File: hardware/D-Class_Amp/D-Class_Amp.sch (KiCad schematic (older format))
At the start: 17 parts, among them J101 AudioJack2, U101 NCP1117-12_TO252, U102 MCP1799T-5002H_TT

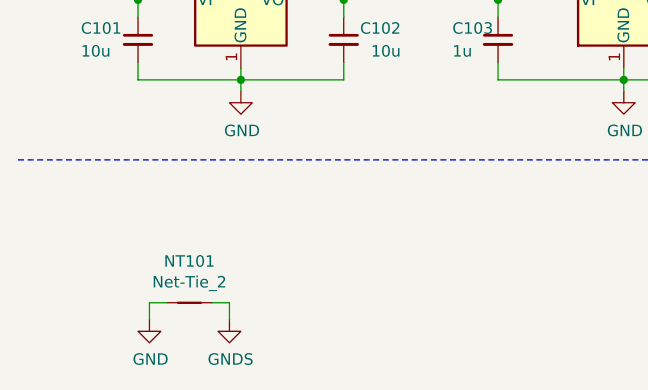
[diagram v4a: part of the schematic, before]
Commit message: updated fet footprints, and added power stage test points
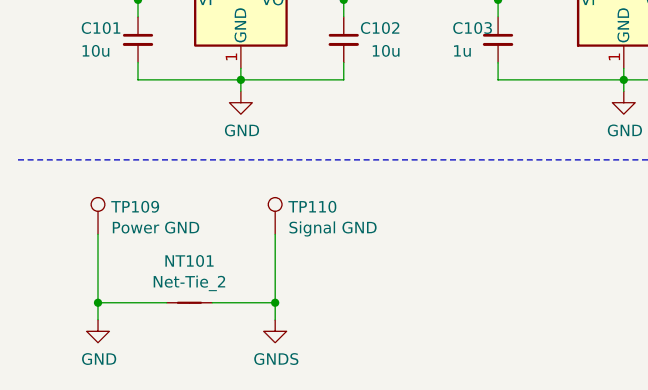
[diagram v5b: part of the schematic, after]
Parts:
- added TP109: Power GND, TestPoint:TestPoint_THTPad_D2.0mm_Drill1.0mm, symbol Connector:TestPoint
- added TP110: Signal GND, TestPoint:TestPoint_THTPad_D2.0mm_Drill1.0mm, symbol Connector:TestPoint
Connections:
- net GND: now also TP109.1
- net GNDS: now also TP110.1
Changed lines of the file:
@@
 L power:GNDS #PWR0102
 U 1 1 612A4FBB
-P 1400 2675
-F 0 "#PWR0102" H 1400 2425 50  0001 C CNN
-F 1 "GNDS" H 1405 2502 50  0000 C CNN
-F 2 "" H 1400 2675 50  0001 C CNN
-F 3 "" H 1400 2675 50  0001 C CNN
-	1    1400 2675
+P 1600 2675
+F 0 "#PWR0102" H 1600 2425 50  0001 C CNN
+F 1 "GNDS" H 1605 2502 50  0000 C CNN
+F 2 "" H 1600 2675 50  0001 C CNN
+F 3 "" H 1600 2675 50  0001 C CNN
+	1    1600 2675
 	1    0    0    -1
 $EndComp
@@
 L power:GND #PWR0101
 U 1 1 612A56C1
-P 1050 2675
-F 0 "#PWR0101" H 1050 2425 50  0001 C CNN
-F 1 "GND" H 1055 2502 50  0000 C CNN
-F 2 "" H 1050 2675 50  0001 C CNN
-F 3 "" H 1050 2675 50  0001 C CNN
-	1    1050 2675
+P 825 2675
+F 0 "#PWR0101" H 825 2425 50  0001 C CNN
+F 1 "GND" H 830 2502 50  0000 C CNN
+F 2 "" H 825 2675 50  0001 C CNN
+F 3 "" H 825 2675 50  0001 C CNN
+	1    825  2675
 	1    0    0    -1
 $EndComp
@@
 $EndComp
 Wire Wire Line
-	1050 2675 1050 2600
-Wire Wire Line
-	1050 2600 1125 2600
-Wire Wire Line
-	1325 2600 1400 2600
-Wire Wire Line
-	1400 2600 1400 2675
+	825  2675 825  2600
+Wire Wire Line
+	825  2600 1125 2600
+Wire Wire Line
+	1325 2600 1600 2600
+Wire Wire Line
+	1600 2600 1600 2675
 $Comp
 L Connector:TestPoint TP101
@@
 Wire Notes Line
 	475  1975 11250 1975
+$Comp
+L Connector:TestPoint TP109
+U 1 1 6113B2E7
+P 825 2300
+F 0 "TP109" H 883 2418 50  0000 L CNN
+F 1 "Power GND" H 883 2327 50  0000 L CNN
+F 2 "TestPoint:TestPoint_THTPad_D2.0mm_Drill1.0mm" H 1025 2300 50  0001 C CNN
+F 3 "~" H 1025 2300 50  0001 C CNN
+	1    825  2300
+	1    0    0    -1
+$EndComp
+$Comp
+L Connector:TestPoint TP110
+U 1 1 6113B863
+P 1600 2300
+F 0 "TP110" H 1658 2418 50  0000 L CNN
+F 1 "Signal GND" H 1658 2327 50  0000 L CNN
+F 2 "TestPoint:TestPoint_THTPad_D2.0mm_Drill1.0mm" H 1800 2300 50  0001 C CNN
+F 3 "~" H 1800 2300 50  0001 C CNN
+	1    1600 2300
+	1    0    0    -1
+$EndComp
+Wire Wire Line
+	825  2300 825  2600
+Connection ~ 825  2600
+Wire Wire Line
+	1600 2300 1600 2600
+Connection ~ 1600 2600
 $EndSCHEMATC

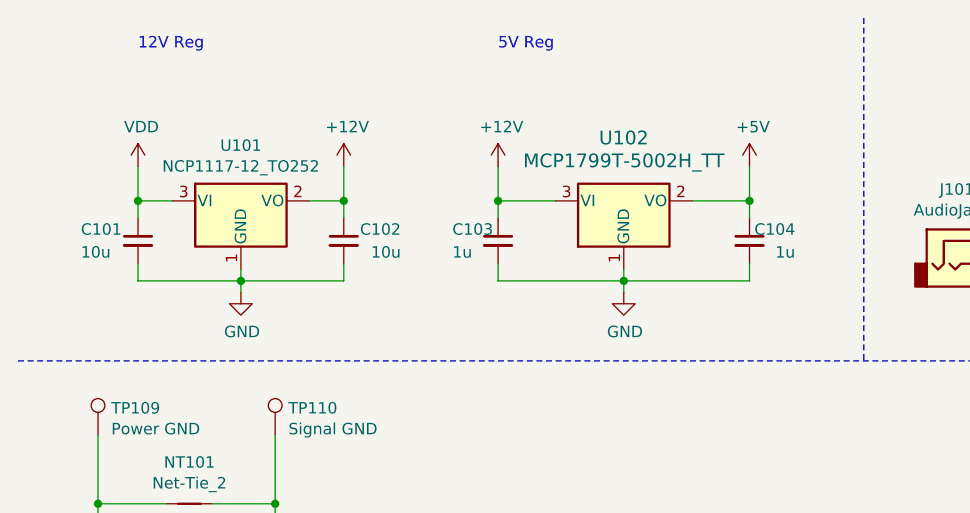
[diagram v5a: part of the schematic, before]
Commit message: Add footprints to the output filter and select output filter components
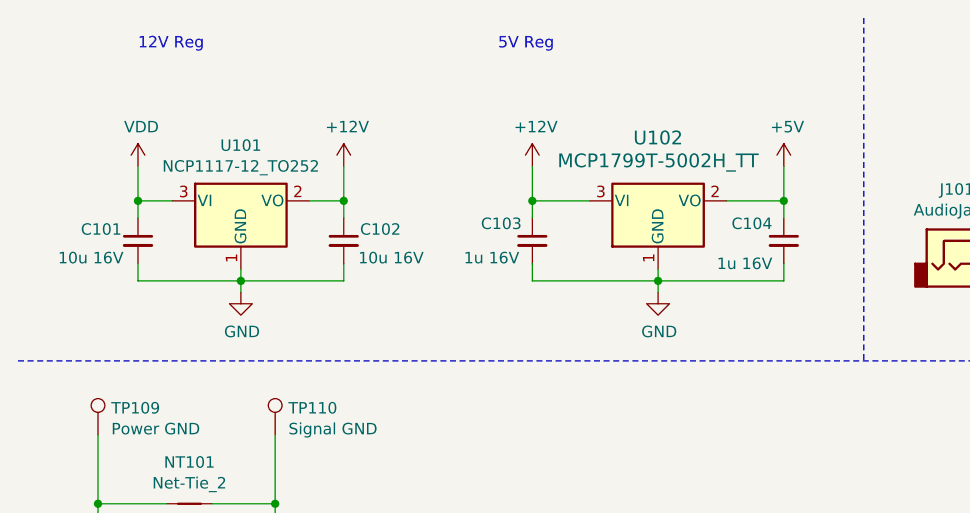
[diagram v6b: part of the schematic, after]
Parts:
- C101, C102: value 10u -> 10u 16V
- C103, C104: value 1u -> 1u 16V
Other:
- moved on the sheet: C103, C104, U102
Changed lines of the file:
@@
 AR Path="/611CA136" Ref="C101"  Part="1"
 F 0 "C101" H 750 1500 50  0000 L CNN
-F 1 "10u" H 750 1400 50  0000 L CNN
+F 1 "10u 16V" H 650 1375 50  0000 L CNN
 F 2 "Capacitor_SMD:C_0805_2012Metric_Pad1.18x1.45mm_HandSolder" H 1000 1450 50  0001 C CNN
 F 3 "~" H 1000 1450 50  0001 C CNN
@@
 AR Path="/611CA13C" Ref="C102"  Part="1"
 F 0 "C102" H 1650 1500 50  0000 L CNN
-F 1 "10u" H 1650 1400 50  0000 L CNN
+F 1 "10u 16V" H 1550 1375 50  0000 L CNN
 F 2 "Capacitor_SMD:C_0805_2012Metric_Pad1.18x1.45mm_HandSolder" H 1900 1450 50  0001 C CNN
 F 3 "~" H 1900 1450 50  0001 C CNN
@@
 L MCP1799T:MCP1799T-5002H_TT U102
 U 1 1 611D89CC
-P 3125 1325
-F 0 "U102" H 3125 1650 60  0000 C CNN
-F 1 "MCP1799T-5002H_TT" H 3125 1550 60  0000 C CNN
-F 2 "Package_TO_SOT_SMD:SOT-23_Handsoldering" H 3925 1565 60  0001 C CNN
-F 3 "" H 3125 1325 60  0000 C CNN
-	1    3125 1325
+P 3275 1325
+F 0 "U102" H 3275 1650 60  0000 C CNN
+F 1 "MCP1799T-5002H_TT" H 3275 1550 60  0000 C CNN
+F 2 "Package_TO_SOT_SMD:SOT-23_Handsoldering" H 4075 1565 60  0001 C CNN
+F 3 "" H 3275 1325 60  0000 C CNN
+	1    3275 1325
 	1    0    0    -1
 $EndComp
@@
 L power:+12V #PWR?
 U 1 1 611E1103
-P 2575 1125
+P 2725 1125
 AR Path="/610497A4/611E1103" Ref="#PWR?"  Part="1"
 AR Path="/611E1103" Ref="#PWR0107"  Part="1"
-F 0 "#PWR0107" H 2575 975 50  0001 C CNN
-F 1 "+12V" H 2590 1298 50  0000 C CNN
-F 2 "" H 2575 1125 50  0001 C CNN
-F 3 "" H 2575 1125 50  0001 C CNN
-	1    2575 1125
+F 0 "#PWR0107" H 2725 975 50  0001 C CNN
+F 1 "+12V" H 2740 1298 50  0000 C CNN
+F 2 "" H 2725 1125 50  0001 C CNN
+F 3 "" H 2725 1125 50  0001 C CNN
+	1    2725 1125
 	1    0    0    -1
 $EndComp
 Wire Wire Line
-	3675 1275 3675 1125
+	3825 1275 3825 1125
 Wire Wire Line
-	3675 1550 3675 1625
-Connection ~ 3675 1275
+	3825 1550 3825 1625
+Connection ~ 3825 1275
 Wire Wire Line
-	3675 1275 3675 1350
+	3825 1275 3825 1350
 $Comp
 L Device:C_Small C?
 U 1 1 611E11B5
-P 3675 1450
+P 3825 1450
 AR Path="/610497A4/611E11B5" Ref="C?"  Part="1"
 AR Path="/611E11B5" Ref="C104"  Part="1"
-F 0 "C104" H 3475 1500 50  0000 L CNN
-F 1 "1u" H 3475 1400 50  0000 L CNN
-F 2 "Capacitor_SMD:C_0805_2012Metric_Pad1.18x1.45mm_HandSolder" H 3675 1450 50  0001 C CNN
-F 3 "~" H 3675 1450 50  0001 C CNN
-	1    3675 1450
+F 0 "C104" H 3875 1525 50  0000 L CNN
+F 1 "1u 16V" H 3875 1350 50  0000 L CNN
+F 2 "Capacitor_SMD:C_0805_2012Metric_Pad1.18x1.45mm_HandSolder" H 3825 1450 50  0001 C CNN
+F 3 "~" H 3825 1450 50  0001 C CNN
+	1    3825 1450
 	-1   0    0    -1
 $EndComp
 Wire Wire Line
-	2575 1275 2575 1125
+	2725 1275 2725 1125
 Wire Wire Line
-	2575 1275 2575 1350
-Connection ~ 2575 1275
+	2725 1275 2725 1350
+Connection ~ 2725 1275
 Wire Wire Line
-	2575 1550 2575 1625
+	2725 1550 2725 1625
 $Comp
 L Device:C_Small C?
 U 1 1 611E56D5
-P 2575 1450
+P 2725 1450
 AR Path="/610497A4/611E56D5" Ref="C?"  Part="1"
 AR Path="/611E56D5" Ref="C103"  Part="1"
-F 0 "C103" H 2375 1500 50  0000 L CNN
-F 1 "1u" H 2375 1400 50  0000 L CNN
-F 2 "Capacitor_SMD:C_0805_2012Metric_Pad1.18x1.45mm_HandSolder" H 2575 1450 50  0001 C CNN
-F 3 "~" H 2575 1450 50  0001 C CNN
-	1    2575 1450
+F 0 "C103" H 2500 1525 50  0000 L CNN
+F 1 "1u 16V" H 2425 1375 50  0000 L CNN
+F 2 "Capacitor_SMD:C_0805_2012Metric_Pad1.18x1.45mm_HandSolder" H 2725 1450 50  0001 C CNN
+F 3 "~" H 2725 1450 50  0001 C CNN
+	1    2725 1450
 	1    0    0    -1
 $EndComp
 Wire Wire Line
-	2575 1625 3125 1625
+	2725 1625 3275 1625
 Wire Wire Line
-	2575 1275 2825 1275
+	2725 1275 2975 1275
 Wire Wire Line
-	3125 1575 3125 1625
-Connection ~ 3125 1625
+	3275 1575 3275 1625
+Connection ~ 3275 1625
 Wire Wire Line
-	3125 1625 3675 1625
+	3275 1625 3825 1625
 Wire Wire Line
-	3425 1275 3675 1275
+	3575 1275 3825 1275
 $Comp
 L power:+5V #PWR0109
 U 1 1 611F0048
-P 3675 1125
-F 0 "#PWR0109" H 3675 975 50  0001 C CNN
-F 1 "+5V" H 3690 1298 50  0000 C CNN
-F 2 "" H 3675 1125 50  0001 C CNN
-F 3 "" H 3675 1125 50  0001 C CNN
-	1    3675 1125
+P 3825 1125
+F 0 "#PWR0109" H 3825 975 50  0001 C CNN
+F 1 "+5V" H 3840 1298 50  0000 C CNN
+F 2 "" H 3825 1125 50  0001 C CNN
+F 3 "" H 3825 1125 50  0001 C CNN
+	1    3825 1125
 	1    0    0    -1
 $EndComp
@@
 L power:GND #PWR?
 U 1 1 611FCDB4
-P 3125 1675
+P 3275 1675
 AR Path="/610497A4/611FCDB4" Ref="#PWR?"  Part="1"
 AR Path="/611FCDB4" Ref="#PWR0108"  Part="1"
-F 0 "#PWR0108" H 3125 1425 50  0001 C CNN
-F 1 "GND" H 3130 1502 50  0000 C CNN
-F 2 "" H 3125 1675 50  0001 C CNN
-F 3 "" H 3125 1675 50  0001 C CNN
-	1    3125 1675
+F 0 "#PWR0108" H 3275 1425 50  0001 C CNN
+F 1 "GND" H 3280 1502 50  0000 C CNN
+F 2 "" H 3275 1675 50  0001 C CNN
+F 3 "" H 3275 1675 50  0001 C CNN
+	1    3275 1675
 	1    0    0    -1
 $EndComp
 Wire Wire Line
-	3125 1625 3125 1675
+	3275 1625 3275 1675
 Wire Notes Line
 	475  1975 11250 1975

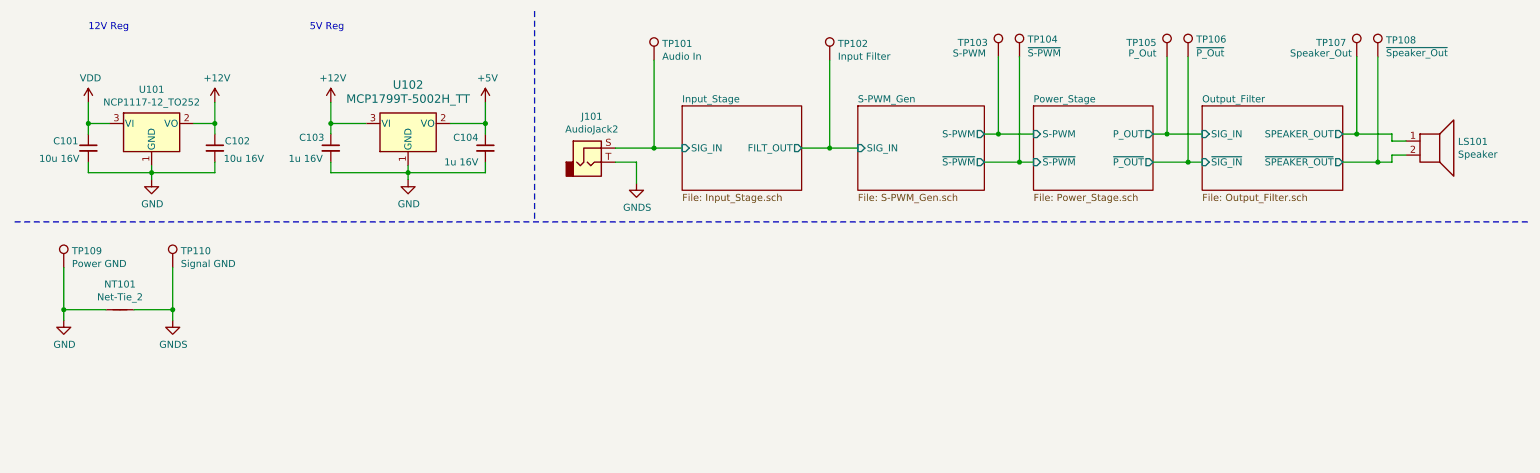
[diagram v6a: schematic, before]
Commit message: added pricing and and part numbers to all components
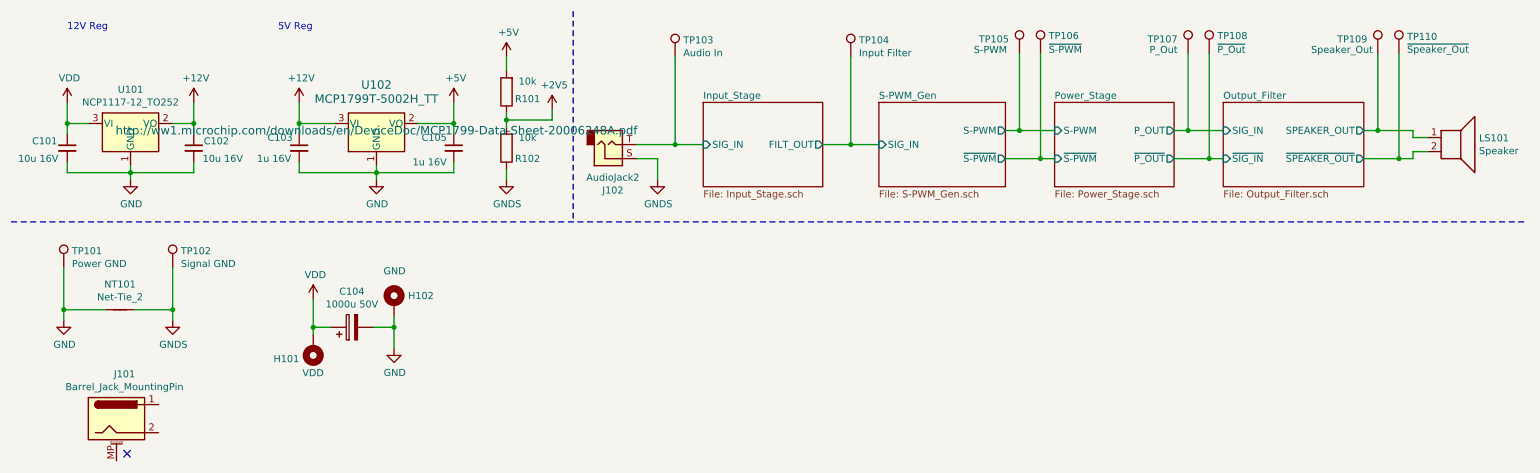
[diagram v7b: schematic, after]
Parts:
- added C104: 1000u 50V, Capacitor_THT:CP_Radial_D10.0mm_P5.00mm, symbol Device:CP
- added H101: VDD, symbol Mechanical:MountingHole_Pad
- added H102: GND, symbol Mechanical:MountingHole_Pad
- added J101: Barrel_Jack_MountingPin, symbol Connector:Barrel_Jack_MountingPin
- added R101, R102: 10k, Resistor_SMD:R_0805_2012Metric_Pad1.20x1.40mm_HandSolder, symbol Device:R
- C101, C102: DigiKey Price (none) -> 0.34; Part Number (none) -> CL21A106KOQNNWE
- C103: DigiKey Price (none) -> 0.16; Part Number (none) -> 885012207051
- C105: renamed from C104; DigiKey Price (none) -> 0.16; Part Number (none) -> 885012207051
- J102: renamed from J101; footprint (none) -> Connector_Audio:Jack_3.5mm_CUI_SJ-3523-SMT_Horizontal
- U101: DigiKey Price (none) -> 1.18; Part Number (none) -> NCP1117DT12G
- U102: DigiKey Price (none) -> 0.62; Part Number (none) -> MCP1799T-5002H/TT
- renumbered TP109 to TP101, TP110 to TP102, TP101 to TP103, TP102 to TP104, TP103 to TP105, TP104 to TP106, TP105 to TP107, TP106 to TP108, TP107 to TP109, TP108 to TP110
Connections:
- net +5V: now also R101.2
- net GND: now also C104.2, H102.1
- net GNDS: now also J102.S, R102.1; no longer J102.T
- net Input_Stage/SIG_IN: now also J102.T; no longer J102.S
- net VDD: now also C104.1, H101.1
- new net +2V5: R101.1, R102.2
- no-connect marks 0 -> 1
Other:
- moved on the sheet: C101, C102, C103, C105, J102, LS101, TP103, TP104, TP105, TP106, TP107, TP108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

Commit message: updated the BOM
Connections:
- no-connect marks 1 -> 0
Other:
- moved on the sheet: C104, H101, H102, J101, NT101, TP101, TP102
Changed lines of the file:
@@
 L power:GNDS #PWR0104
 U 1 1 612A4FBB
-P 1600 2675
-F 0 "#PWR0104" H 1600 2425 50  0001 C CNN
-F 1 "GNDS" H 1605 2502 50  0000 C CNN
-F 2 "" H 1600 2675 50  0001 C CNN
-F 3 "" H 1600 2675 50  0001 C CNN
-	1    1600 2675
+P 1675 2675
+F 0 "#PWR0104" H 1675 2425 50  0001 C CNN
+F 1 "GNDS" H 1680 2502 50  0000 C CNN
+F 2 "" H 1675 2675 50  0001 C CNN
+F 3 "" H 1675 2675 50  0001 C CNN
+	1    1675 2675
 	1    0    0    -1
 $EndComp
@@
 L power:GND #PWR0101
 U 1 1 612A56C1
-P 825 2675
-F 0 "#PWR0101" H 825 2425 50  0001 C CNN
-F 1 "GND" H 830 2502 50  0000 C CNN
-F 2 "" H 825 2675 50  0001 C CNN
-F 3 "" H 825 2675 50  0001 C CNN
-	1    825  2675
+P 900 2675
+F 0 "#PWR0101" H 900 2425 50  0001 C CNN
+F 1 "GND" H 905 2502 50  0000 C CNN
+F 2 "" H 900 2675 50  0001 C CNN
+F 3 "" H 900 2675 50  0001 C CNN
+	1    900  2675
 	1    0    0    -1
 $EndComp
@@
 L Device:Net-Tie_2 NT101
 U 1 1 612A676E
-P 1225 2600
-F 0 "NT101" H 1225 2781 50  0000 C CNN
-F 1 "Net-Tie_2" H 1225 2690 50  0000 C CNN
-F 2 "" H 1225 2600 50  0001 C CNN
-F 3 "~" H 1225 2600 50  0001 C CNN
-	1    1225 2600
-	1    0    0    -1
-$EndComp
-Wire Wire Line
-	825  2675 825  2600
-Wire Wire Line
-	825  2600 1125 2600
-Wire Wire Line
-	1325 2600 1600 2600
-Wire Wire Line
-	1600 2600 1600 2675
+P 1300 2600
+F 0 "NT101" H 1300 2781 50  0000 C CNN
+F 1 "Net-Tie_2" H 1300 2690 50  0000 C CNN
+F 2 "" H 1300 2600 50  0001 C CNN
+F 3 "~" H 1300 2600 50  0001 C CNN
+	1    1300 2600
+	1    0    0    -1
+$EndComp
+Wire Wire Line
+	900  2675 900  2600
+Wire Wire Line
+	900  2600 1200 2600
+Wire Wire Line
+	1400 2600 1675 2600
+Wire Wire Line
+	1675 2600 1675 2675
 $Comp
 L Connector:TestPoint TP103
@@
 F 1 "MCP1799T-5002H_TT" H 3050 1550 60  0000 C CNN
 F 2 "Package_TO_SOT_SMD:SOT-23_Handsoldering" H 3850 1565 60  0001 C CNN
-F 3 "http://ww1.microchip.com/downloads/en/DeviceDoc/MCP1799-Data-Sheet-20006248A.pdf" H 3050 1325 60  0000 C CNN
+F 3 "http://ww1.microchip.com/downloads/en/DeviceDoc/MCP1799-Data-Sheet-20006248A.pdf" H 3050 1325 60  0001 C CNN
 F 4 "0.62" H 3050 1325 50  0001 C CNN "DigiKey Price"
 F 5 "MCP1799T-5002H/TT" H 3050 1325 50  0001 C CNN "Part Number"
@@
 L Connector:TestPoint TP101
 U 1 1 6113B2E7
-P 825 2300
-F 0 "TP101" H 883 2418 50  0000 L CNN
-F 1 "Power GND" H 883 2327 50  0000 L CNN
-F 2 "TestPoint:TestPoint_THTPad_D2.0mm_Drill1.0mm" H 1025 2300 50  0001 C CNN
-F 3 "~" H 1025 2300 50  0001 C CNN
-	1    825  2300
+P 900 2300
+F 0 "TP101" H 958 2418 50  0000 L CNN
+F 1 "Power GND" H 958 2327 50  0000 L CNN
+F 2 "TestPoint:TestPoint_THTPad_D2.0mm_Drill1.0mm" H 1100 2300 50  0001 C CNN
+F 3 "~" H 1100 2300 50  0001 C CNN
+	1    900  2300
 	1    0    0    -1
 $EndComp
@@
 L Connector:TestPoint TP102
 U 1 1 6113B863
-P 1600 2300
-F 0 "TP102" H 1658 2418 50  0000 L CNN
-F 1 "Signal GND" H 1658 2327 50  0000 L CNN
-F 2 "TestPoint:TestPoint_THTPad_D2.0mm_Drill1.0mm" H 1800 2300 50  0001 C CNN
-F 3 "~" H 1800 2300 50  0001 C CNN
-	1    1600 2300
-	1    0    0    -1
-$EndComp
-Wire Wire Line
-	825  2300 825  2600
-Connection ~ 825  2600
-Wire Wire Line
-	1600 2300 1600 2600
-Connection ~ 1600 2600
+P 1675 2300
+F 0 "TP102" H 1733 2418 50  0000 L CNN
+F 1 "Signal GND" H 1733 2327 50  0000 L CNN
+F 2 "TestPoint:TestPoint_THTPad_D2.0mm_Drill1.0mm" H 1875 2300 50  0001 C CNN
+F 3 "~" H 1875 2300 50  0001 C CNN
+	1    1675 2300
+	1    0    0    -1
+$EndComp
+Wire Wire Line
+	900  2300 900  2600
+Connection ~ 900  2600
+Wire Wire Line
+	1675 2300 1675 2600
+Connection ~ 1675 2600
 Wire Wire Line
 	3975 1600 3975 1675
@@
 	3975 1250 4300 1250
 $Comp
+L Mechanical:MountingHole_Pad H102
+U 1 1 6126D650
+P 3325 2375
+F 0 "H102" H 3425 2424 50  0000 L CNN
+F 1 "GND" H 3250 2600 50  0000 L CNN
+F 2 "" H 3325 2375 50  0001 C CNN
+F 3 "~" H 3325 2375 50  0001 C CNN
+	1    3325 2375
+	1    0    0    -1
+$EndComp
+$Comp
+L power:GND #PWR0109
+U 1 1 6127C8B5
+P 3325 2700
+F 0 "#PWR0109" H 3325 2450 50  0001 C CNN
+F 1 "GND" H 3330 2527 50  0000 C CNN
+F 2 "" H 3325 2700 50  0001 C CNN
+F 3 "" H 3325 2700 50  0001 C CNN
+	1    3325 2700
+	1    0    0    -1
+$EndComp
+Wire Wire Line
+	3325 2700 3325 2550
+$Comp
+L Device:CP C104
+U 1 1 6127F37C
+P 3025 2550
+F 0 "C104" V 3280 2550 50  0000 C CNN
+F 1 "1000u 50V" V 3189 2550 50  0000 C CNN
+F 2 "Capacitor_THT:CP_Radial_D10.0mm_P5.00mm" H 3063 2400 50  0001 C CNN
+F 3 "~" H 3025 2550 50  0001 C CNN
+F 4 "1" H 3025 2550 50  0001 C CNN "DigiKey Price"
+	1    3025 2550
+	0    -1   -1   0
+$EndComp
+Wire Wire Line
+	3175 2550 3325 2550
+Connection ~ 3325 2550
+Wire Wire Line
+	3325 2550 3325 2475
+$Comp
+L power:VDD #PWR?
+U 1 1 612997D9
+P 2750 2350
+AR Path="/610497A4/612997D9" Ref="#PWR?"  Part="1"
+AR Path="/612997D9" Ref="#PWR0107"  Part="1"
+F 0 "#PWR0107" H 2750 2200 50  0001 C CNN
+F 1 "VDD" H 2765 2523 50  0000 C CNN
+F 2 "" H 2750 2350 50  0001 C CNN
+F 3 "" H 2750 2350 50  0001 C CNN
+	1    2750 2350
+	1    0    0    -1
+$EndComp
+$Comp
+L Mechanical:MountingHole_Pad H101
+U 1 1 6126CC33
+P 2750 2700
+F 0 "H101" H 2850 2775 50  0000 L CNN
+F 1 "VDD" H 2675 2875 50  0000 L CNN
+F 2 "" H 2750 2700 50  0001 C CNN
+F 3 "~" H 2750 2700 50  0001 C CNN
+	1    2750 2700
+	-1   0    0    1
+$EndComp
+Wire Wire Line
+	2750 2350 2750 2550
+Connection ~ 2750 2550
+Wire Wire Line
+	2750 2600 2750 2550
+Wire Wire Line
+	2750 2550 2875 2550
+$Comp
 L Connector:Barrel_Jack_MountingPin J101
 U 1 1 612622C7
-P 1200 3375
-F 0 "J101" H 1257 3692 50  0000 C CNN
-F 1 "Barrel_Jack_MountingPin" H 1257 3601 50  0000 C CNN
-F 2 "" H 1250 3335 50  0001 C CNN
-F 3 "~" H 1250 3335 50  0001 C CNN
-	1    1200 3375
-	1    0    0    -1
-$EndComp
-NoConn ~ 1275 3625
-$Comp
-L Mechanical:MountingHole_Pad H102
-U 1 1 6126D650
-P 3175 2550
-F 0 "H102" H 3275 2599 50  0000 L CNN
-F 1 "GND" H 3100 2775 50  0000 L CNN
-F 2 "" H 3175 2550 50  0001 C CNN
-F 3 "~" H 3175 2550 50  0001 C CNN
-	1    3175 2550
-	1    0    0    -1
-$EndComp
-$Comp
-L power:GND #PWR0109
-U 1 1 6127C8B5
-P 3175 2875
-F 0 "#PWR0109" H 3175 2625 50  0001 C CNN
-F 1 "GND" H 3180 2702 50  0000 C CNN
-F 2 "" H 3175 2875 50  0001 C CNN
-F 3 "" H 3175 2875 50  0001 C CNN
-	1    3175 2875
-	1    0    0    -1
-$EndComp
-Wire Wire Line
-	3175 2875 3175 2725
-$Comp
-L Device:CP C104
-U 1 1 6127F37C
-P 2875 2725
-F 0 "C104" V 3130 2725 50  0000 C CNN
-F 1 "1000u 50V" V 3039 2725 50  0000 C CNN
-F 2 "Capacitor_THT:CP_Radial_D10.0mm_P5.00mm" H 2913 2575 50  0001 C CNN
-F 3 "~" H 2875 2725 50  0001 C CNN
-F 4 "1" H 2875 2725 50  0001 C CNN "DigiKey Price"
-	1    2875 2725
-	0    -1   -1   0
-$EndComp
-Wire Wire Line
-	3025 2725 3175 2725
-Connection ~ 3175 2725
-Wire Wire Line
-	3175 2725 3175 2650
-$Comp
-L power:VDD #PWR?
-U 1 1 612997D9
-P 2600 2525
-AR Path="/610497A4/612997D9" Ref="#PWR?"  Part="1"
-AR Path="/612997D9" Ref="#PWR0107"  Part="1"
-F 0 "#PWR0107" H 2600 2375 50  0001 C CNN
-F 1 "VDD" H 2615 2698 50  0000 C CNN
-F 2 "" H 2600 2525 50  0001 C CNN
-F 3 "" H 2600 2525 50  0001 C CNN
-	1    2600 2525
-	1    0    0    -1
-$EndComp
-$Comp
-L Mechanical:MountingHole_Pad H101
-U 1 1 6126CC33
-P 2600 2875
-F 0 "H101" H 2700 2950 50  0000 L CNN
-F 1 "VDD" H 2525 3050 50  0000 L CNN
-F 2 "" H 2600 2875 50  0001 C CNN
-F 3 "~" H 2600 2875 50  0001 C CNN
-	1    2600 2875
-	-1   0    0    1
-$EndComp
-Wire Wire Line
-	2600 2525 2600 2725
-Connection ~ 2600 2725
-Wire Wire Line
-	2600 2775 2600 2725
-Wire Wire Line
-	2600 2725 2725 2725
+P 4450 2550
+F 0 "J101" H 4450 2875 50  0000 C CNN
+F 1 "Barrel_Jack_MountingPin" H 4507 2776 50  0000 C CNN
+F 2 "" H 4500 2510 50  0001 C CNN
+F 3 "~" H 4500 2510 50  0001 C CNN
+	1    4450 2550
+	1    0    0    -1
+$EndComp
 $EndSCHEMATC
